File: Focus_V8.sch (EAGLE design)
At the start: 103 parts

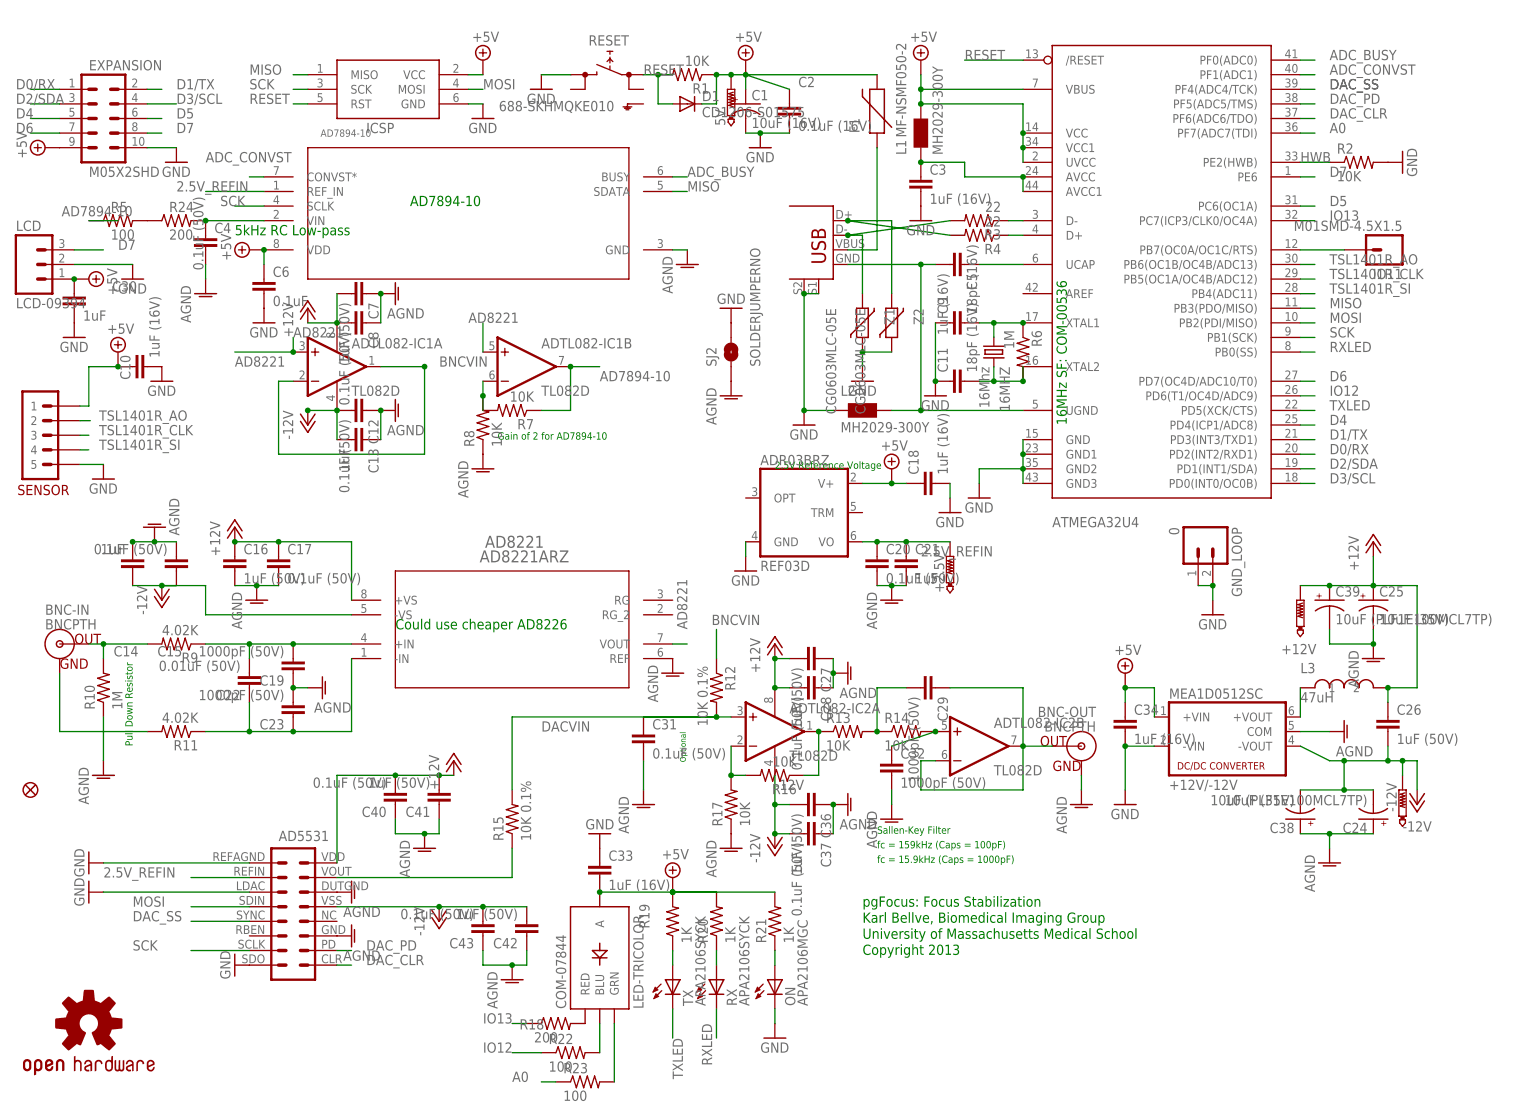
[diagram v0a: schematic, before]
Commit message: Change connection between analog and digital ground plans via a cutable trace, which means that both ground planes will be connected by default.
Also pin 6 (RBEN) of AD5531 was mistakenly left floating, now connected to 5V line to
force deactivation.
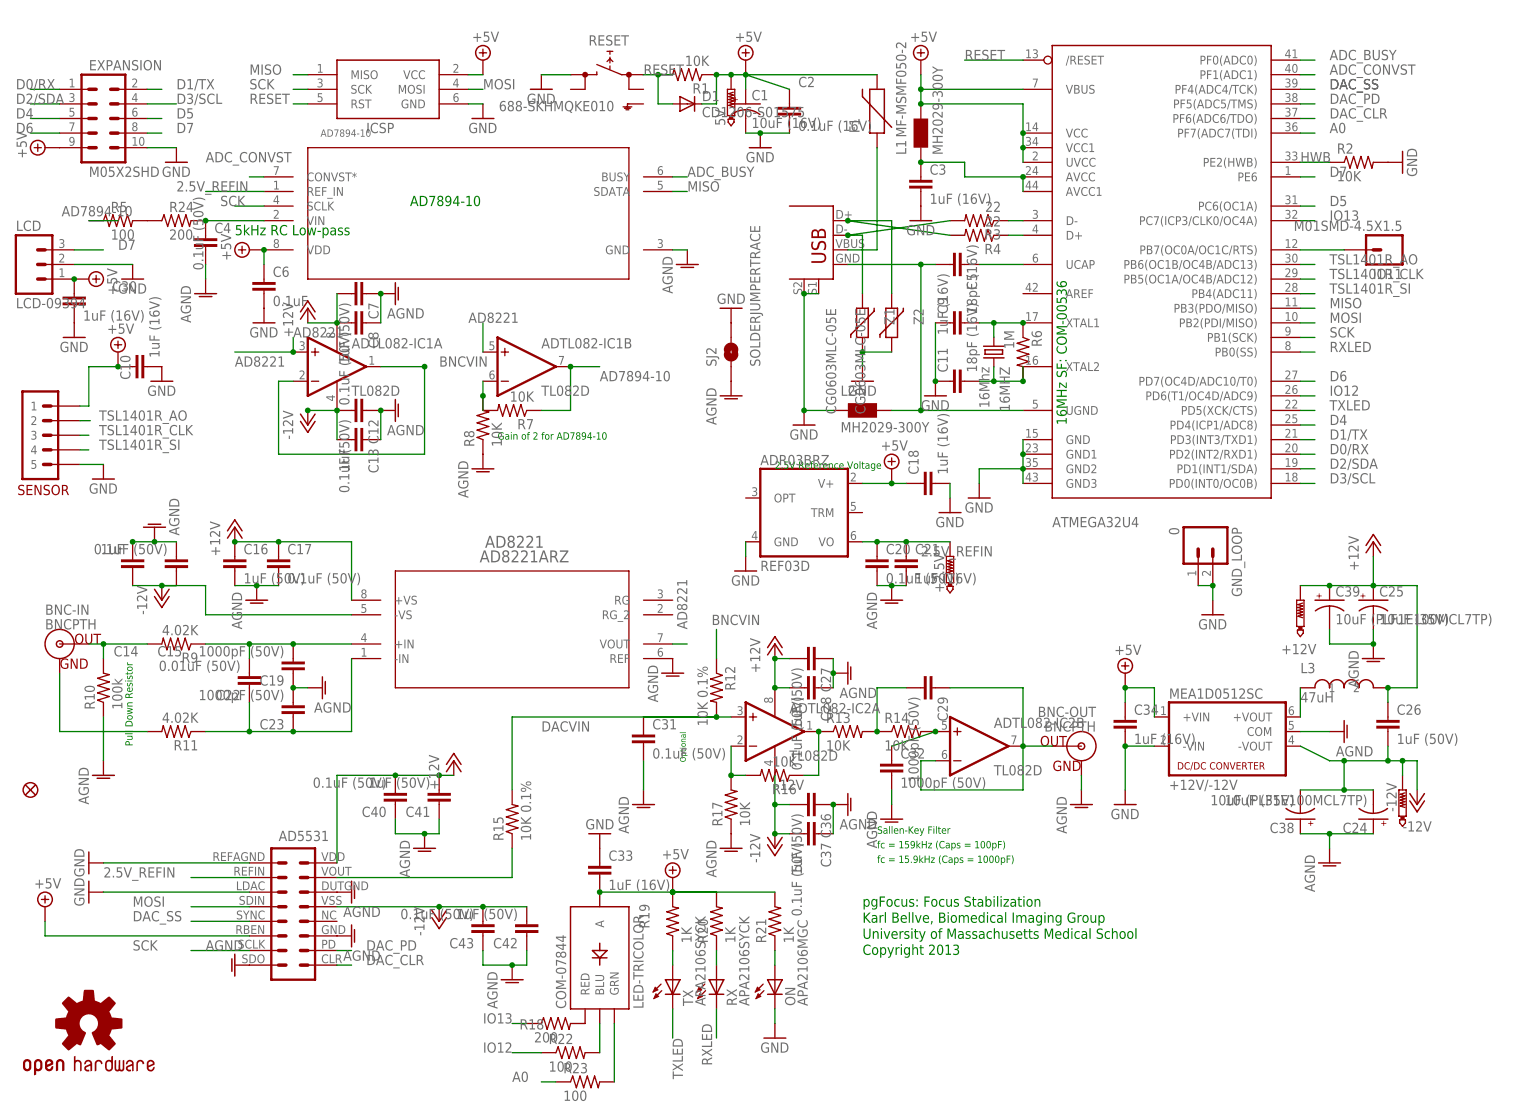
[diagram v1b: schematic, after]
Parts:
- C21, C30: value 1uF -> 1uF (16V)
- F1: value MF-NSMF050-2 -> MF-MSMF050-2
- R10: value 1M -> 100k
- SJ2: value SOLDERJUMPERNO -> SOLDERJUMPERTRACE; device SparkFun-Passives:SOLDERJUMPERNO -> SparkFun-Passives:SOLDERJUMPERTRACE
- U$1: value AD5331 -> AD5531
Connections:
- net +5V: now also U$1.RBEN
- net AGND: now also U$1.SDO
- net GND: no longer U$1.SDO
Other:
- note removed: "Could use cheaper AD8226"
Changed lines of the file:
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@@
 <part name="C17" library="SparkFun" deviceset="CAP" device="0603-CAP" value="0.1uF (50V)"/>
 <part name="BNC-OUT" library="SparkFun" deviceset="BNC" device="PTH"/>
-<part name="R10" library="SparkFun" deviceset="RESISTOR" device="0603-RES" value="1M"/>
+<part name="R10" library="SparkFun" deviceset="RESISTOR" device="0603-RES" value="100k"/>
 <part name="C18" library="SparkFun" deviceset="CAP" device="0603-CAP" value="1uF (16V)"/>
 <part name="16MHZ" library="SparkFun" deviceset="CRYSTAL" device="HC49UV" value="16Mhz"/>
@@
 <part name="GND30" library="supply1" deviceset="AGND" device=""/>
 <part name="GND31" library="supply1" deviceset="AGND" device=""/>
-<part name="C21" library="SparkFun" deviceset="CAP" device="0603-CAP" value="1uF"/>
+<part name="C21" library="SparkFun" deviceset="CAP" device="0603-CAP" value="1uF (16V)"/>
 <part name="GND28" library="SparkFun" deviceset="GND" device=""/>
 <part name="Z2" library="varistor" deviceset="VARISTOR" device="CN0603" value="CG0603MLC-05E"/>
 <part name="Z1" library="varistor" deviceset="VARISTOR" device="CN0603" value="CG0603MLC-05E"/>
 <part name="L2" library="wuerth-elektronik" deviceset="WE-CBF" device="_0805" value="MH2029-300Y"/>
-<part name="F1" library="SparkFun" deviceset="PTC" device="SMD" value="MF-NSMF050-2"/>
+<part name="F1" library="SparkFun" deviceset="PTC" device="SMD" value="MF-MSMF050-2"/>
 <part name="C4" library="SparkFun" deviceset="CAP" device="0603-CAP" value="0.1uF (50V)"/>
 <part name="GND3" library="supply1" deviceset="AGND" device=""/>
@@
 <part name="GND45" library="supply1" deviceset="AGND" device=""/>
 <part name="GND46" library="SparkFun" deviceset="GND" device=""/>
-<part name="SJ2" library="SparkFun-Passives" deviceset="SOLDERJUMPER" device="NO"/>
+<part name="SJ2" library="SparkFun-Passives" deviceset="SOLDERJUMPER" device="TRACE" value="SOLDERJUMPERTRACE"/>
 <part name="LCD" library="SparkFun-Connectors" deviceset="M03" device="JST-PTH" value="LCD-09394"/>
-<part name="C30" library="SparkFun" deviceset="CAP" device="0603-CAP" value="1uF"/>
+<part name="C30" library="SparkFun" deviceset="CAP" device="0603-CAP" value="1uF (16V)"/>
 <part name="GND47" library="SparkFun" deviceset="GND" device=""/>
 <part name="SUPPLY19" library="supply2" deviceset="+5V" device=""/>
@@
 <part name="IO11" library="SparkFun-Connectors" deviceset="M01" device="SMD-4.5X1.5"/>
 <part name="GND18" library="SparkFun" deviceset="GND" device=""/>
-<part name="U$1" library="BIG" deviceset="AD5331" device=""/>
-<part name="GND20" library="SparkFun" deviceset="GND" device=""/>
+<part name="U$1" library="BIG" deviceset="AD5331" device="" value="AD5531"/>
 <part name="GND49" library="supply1" deviceset="AGND" device=""/>
 <part name="GND50" library="supply1" deviceset="AGND" device=""/>
@@
 <part name="C39" library="SparkFun-Passives" deviceset="CAP_POL" device="PTH1" value="10uF (PLF1E100MCL7TP)"/>
 <part name="C24" library="SparkFun-Passives" deviceset="CAP_POL" device="PTH1" value="10uF (PLF1E100MCL7TP)"/>
+<part name="SUPPLY21" library="supply2" deviceset="+5V" device=""/>
+<part name="GND20" library="supply1" deviceset="AGND" device=""/>
 </parts>
 <sheets>
@@
 <text x="93.98" y="50.8" size="1.27" layer="91">Sallen-Key Filter</text>
 <text x="93.98" y="48.26" size="1.27" layer="91">fc = 159kHz (Caps = 100pF)</text>
-<text x="10.16" y="86.36" size="1.778" layer="91">Could use cheaper AD8226</text>
 <text x="93.98" y="45.72" size="1.27" layer="91">fc = 15.9kHz (Caps = 1000pF)</text>
 <text x="91.44" y="35.306" size="1.778" layer="91">Karl Bellve, Biomedical Imaging Group</text>
@@
 <instance part="GND18" gate="1" x="-30.48" y="129.54"/>
 <instance part="U$1" gate="G$1" x="-7.62" y="35.56"/>
-<instance part="GND20" gate="1" x="-17.78" y="27.94" rot="R270"/>
 <instance part="GND49" gate="VR1" x="58.42" y="78.74"/>
 <instance part="GND50" gate="VR1" x="2.54" y="40.64" rot="R90"/>
@@
 <instance part="C39" gate="G$1" x="172.72" y="91.44"/>
 <instance part="C24" gate="G$1" x="180.34" y="53.34" rot="R180"/>
+<instance part="SUPPLY21" gate="+5V" x="-50.8" y="38.1"/>
+<instance part="GND20" gate="VR1" x="-17.78" y="27.94" rot="R270"/>
 </instances>
 <busses>
@@
 <pinref part="GND28" gate="1" pin="GND"/>
 <wire x1="-40.64" y1="40.64" x2="-15.24" y2="40.64" width="0.1524" layer="91"/>
-</segment>
-<segment>
-<pinref part="U$1" gate="G$1" pin="SDO"/>
-<pinref part="GND20" gate="1" pin="GND"/>
 </segment>
 <segment>
@@
 <pinref part="SENSOR" gate="G$1" pin="1"/>
 </segment>
+<segment>
+<pinref part="U$1" gate="G$1" pin="RBEN"/>
+<pinref part="SUPPLY21" gate="+5V" pin="+5V"/>
+<wire x1="-15.24" y1="33.02" x2="-50.8" y2="33.02" width="0.1524" layer="91"/>
+<wire x1="-50.8" y1="33.02" x2="-50.8" y2="35.56" width="0.1524" layer="91"/>
+</segment>
 </net>
 <net name="2.5V_REFIN" class="0">
@@
 <pinref part="GND50" gate="VR1" pin="AGND"/>
 </segment>
-</net>
+<segment>
+<pinref part="U$1" gate="G$1" pin="SDO"/>
+<pinref part="GND20" gate="VR1" pin="AGND"/>
+</segment>
+</net>

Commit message: Updating to eliminate serial LCD connector, and to make a horizontal expansion possible. This simplifies using a box to contain the PCB
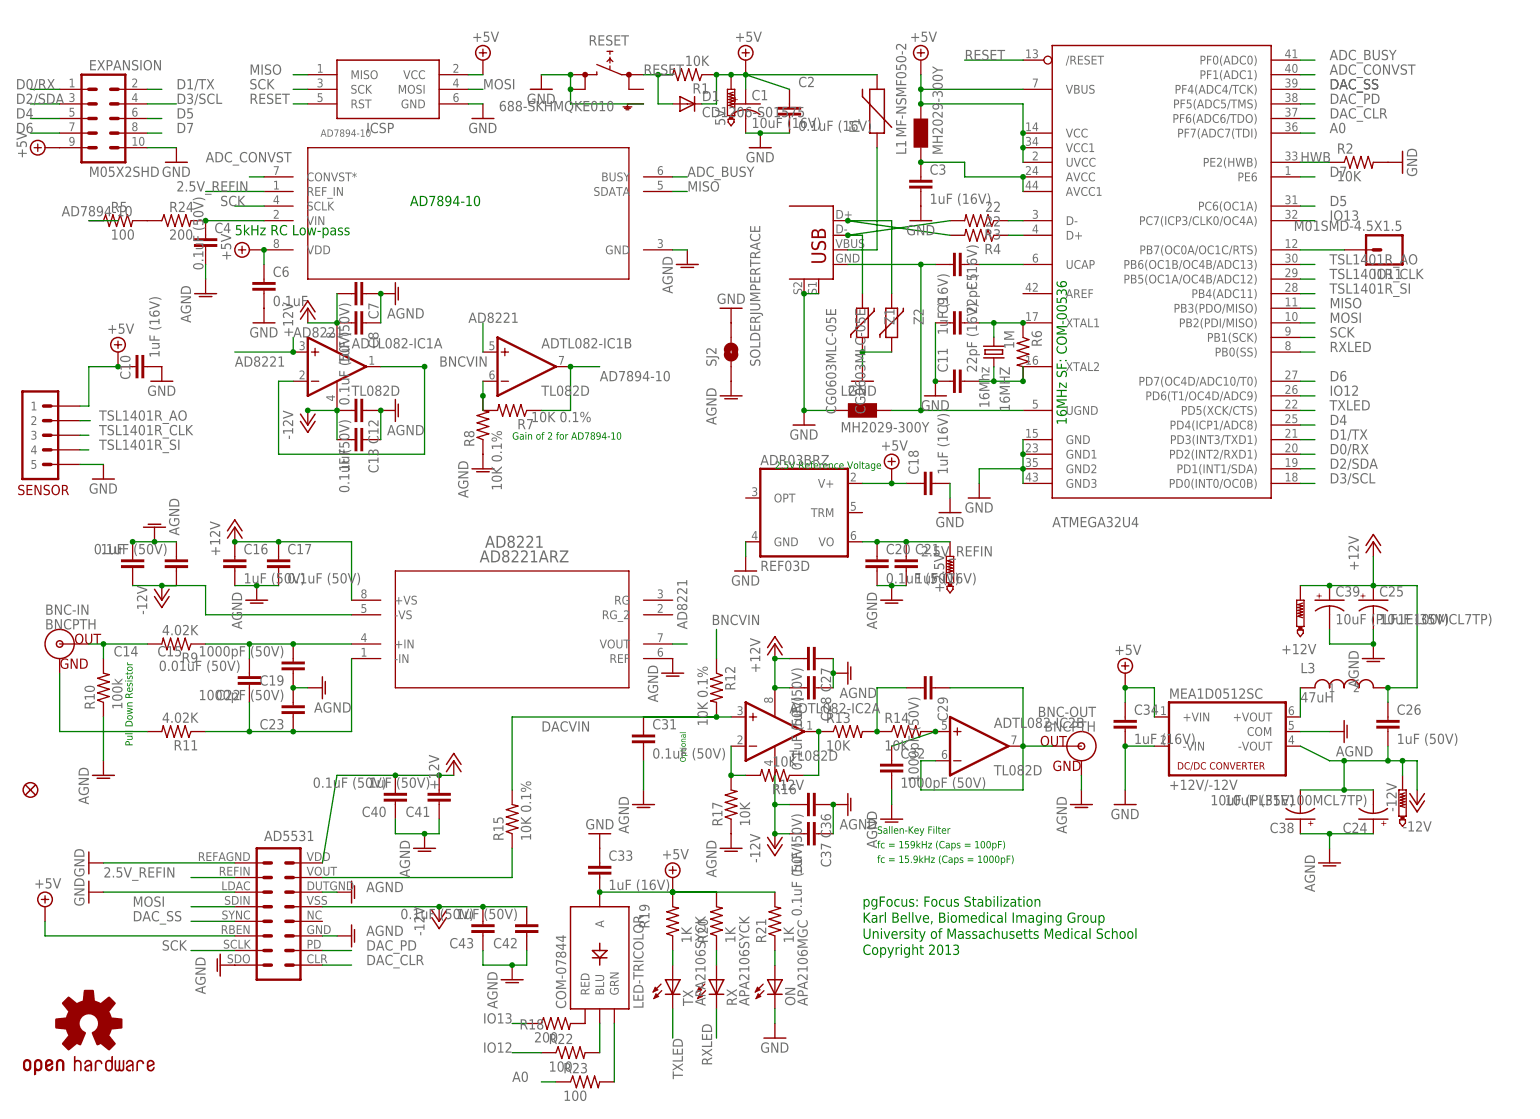
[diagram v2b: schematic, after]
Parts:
- removed C30: 1uF (16V), SparkFun:CAP0603-CAP
- removed GND_LOOP: 0, SparkFun:M02NG
- removed LCD: LCD-09394, SparkFun-Connectors:M03JST-PTH
- C11, C9: value 18pF (16V) -> 22pF (16V)
- F1: value MF-MSMF050-2 -> MF-NSMF050-2
- R7, R8: value 10K -> 10K 0.1%
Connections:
- net +5V: no longer C30.1, LCD.1
- net D7: no longer LCD.3
- net GND: now also RESET.2.2, RESET.SH; no longer C30.2, GND_LOOP.1, GND_LOOP.2, LCD.2
